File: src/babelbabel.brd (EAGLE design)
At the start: 41 x 75.5 mm, 150 parts, among them CON1 CON-4P-TABS-JST_GH-RA, CON10 CON-6P-SM06B, CON101 PINHEAD_1X04-2.54, CON102 PINHEAD_1X03-2.54, CON11 PINHEAD_1X04-2.54, CON12 PINHEAD_1X06-2.54, CON15 PINHEAD_1X04-2.54, CON16 CON-4P-TABS-JST_GH-RA, CON2 PINHEAD_1X04-2.54, CON201 PINHEAD_1X04-2.54, CON202 PINHEAD_1X03-2.54, CON3 PINHEAD_1X04-2.54, CON4 USB-AA-PTH, CON5 CON-4P-TABS-JST_GH-RA, CON6 CON-4P-TABS-JST_GH-RA, CON7 USB-1, IC1 NS5B1G385, IC101 STM32F373CBT6-LQFP48, IC102 STM32F373RCT6, IC103 AP2127-3.3, IC105 TJA1051-SO8, IC108 TPD3S014DBVR-SOT23-6, IC13 STM32F103CBT7, IC14 74LVC2T45, IC15 74LVC2T45, IC16 74LVC2T45, IC17 74LVC2T45, IC2 NS5B1G385, IC201 STM32F373CBT6-LQFP48, IC202 STM32F373RCT6, IC203 AP2127-3.3, IC205 TJA1051-SO8, IC208 TPD3S014DBVR-SOT23-6, IC3 AP2127-3.3, IC9 FE1.1S, J1 CONNECTION-SMD, J2 CONNECTION-SMD, Q101 16MHz, Q102 2N7002, Q201 16MHz, Q202 2N7002, Q7 8MHz, Q8 12MHz, Q9 NTZD3152PT1G

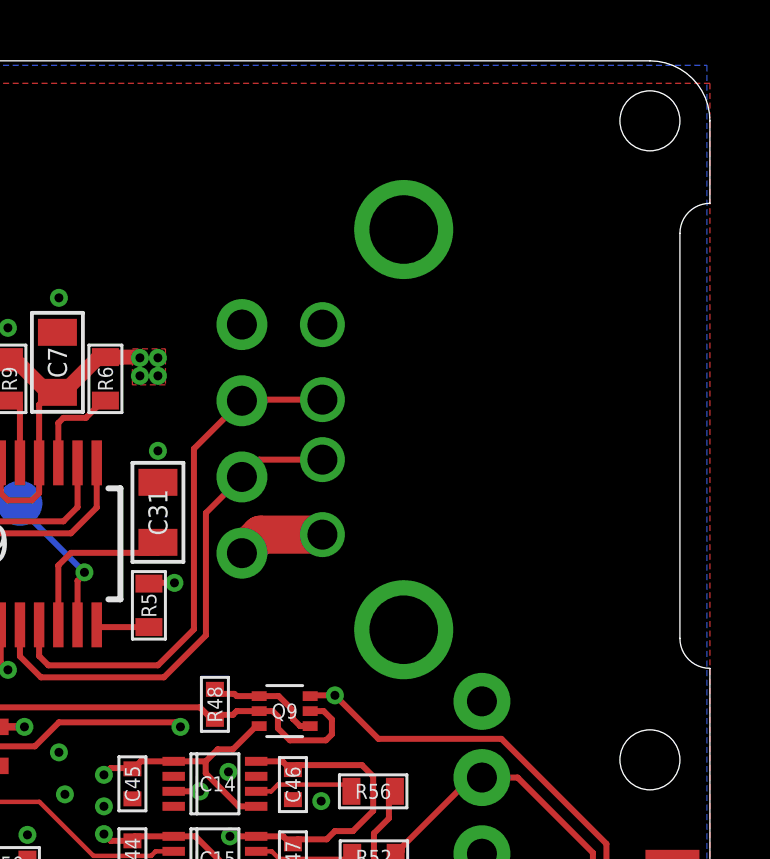
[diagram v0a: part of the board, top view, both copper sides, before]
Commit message: fixed wrong USB connection
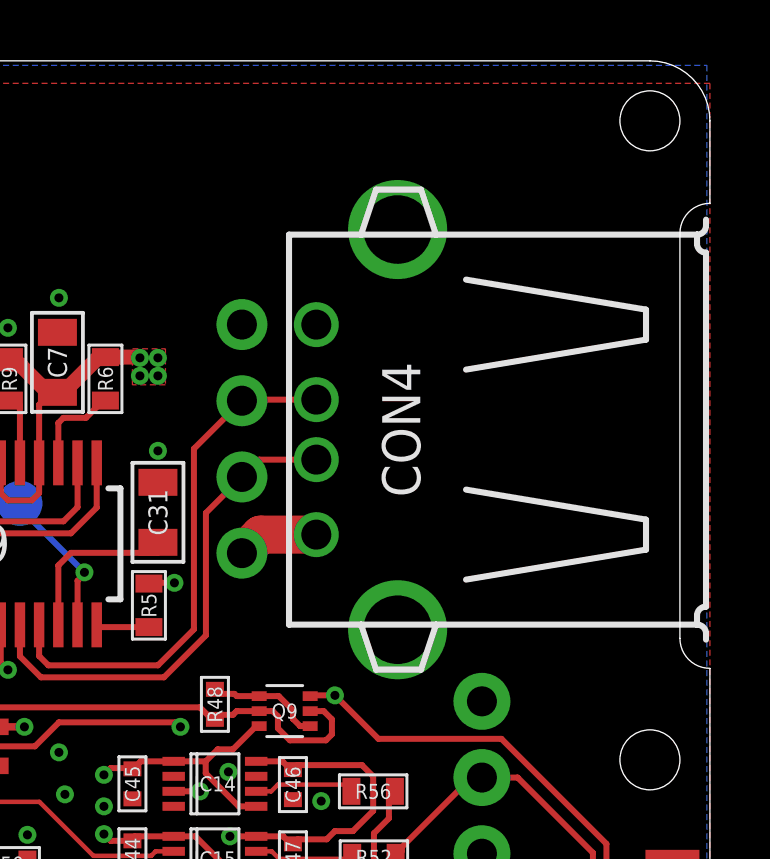
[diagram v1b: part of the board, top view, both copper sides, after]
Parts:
- moved CON4 0.20 mm to (33.2, 25.5), flipped to the top, turned to 90 degrees
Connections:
- net DUT_DM: now also CON4.D-; no longer CON4.D+
- net DUT_DP: now also CON4.D+; no longer CON4.D-
- net GND: now also CON4.GND; no longer CON4.VBUS
- net VDD_5V: now also CON4.VBUS; no longer CON4.GND

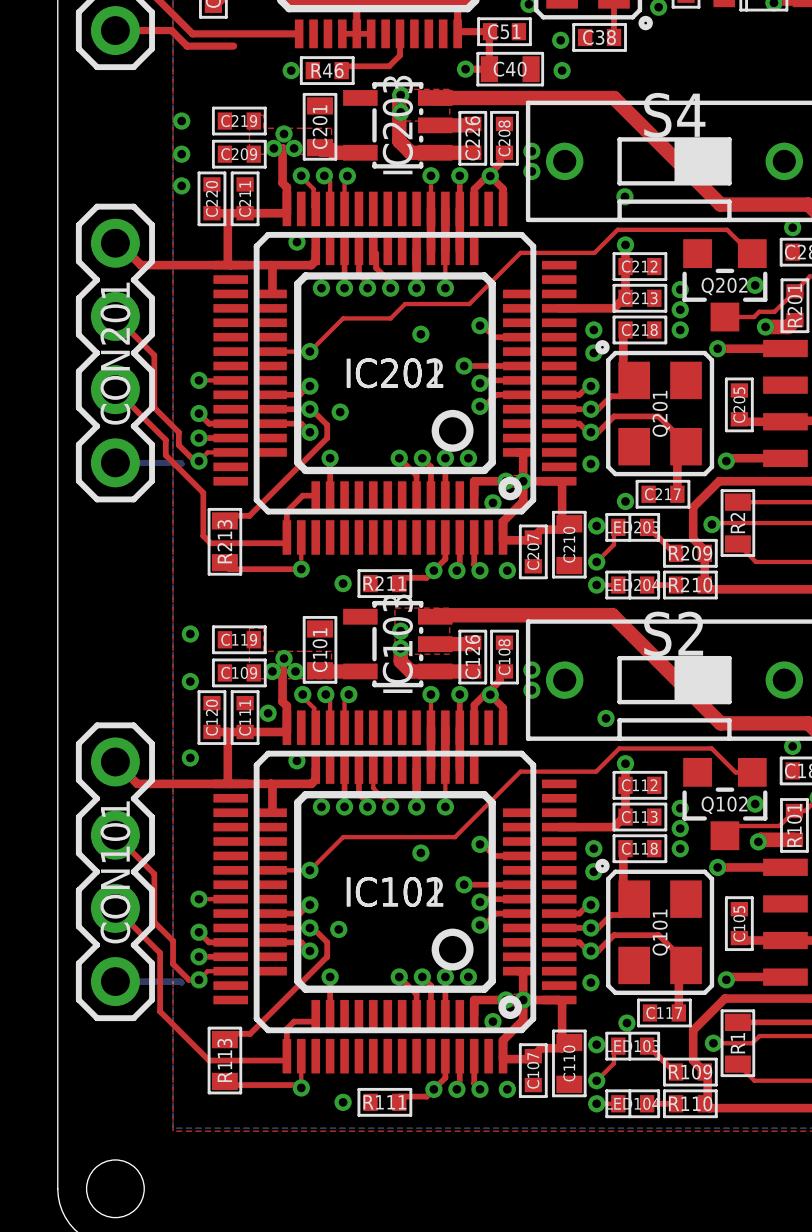
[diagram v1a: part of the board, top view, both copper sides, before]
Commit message: 64 pin swaped with 48
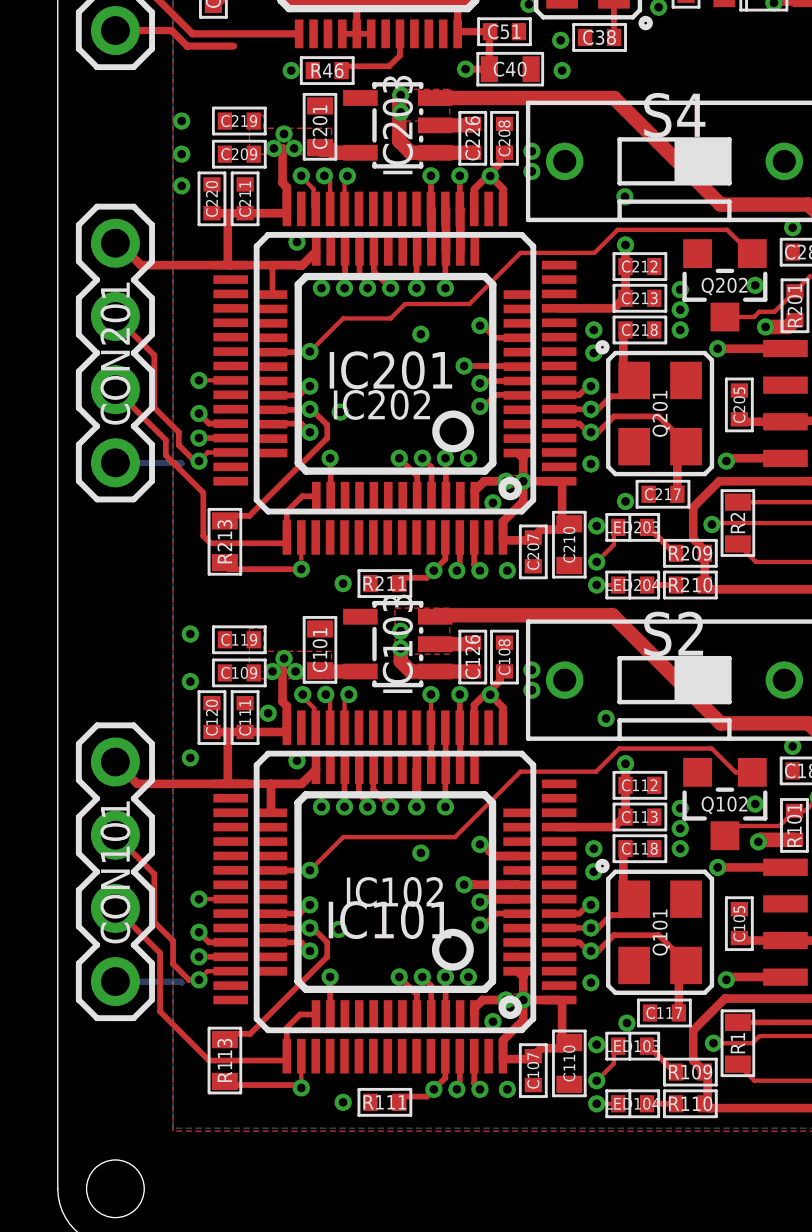
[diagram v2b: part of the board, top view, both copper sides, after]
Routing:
- net BABEL1:PA4: track 25.5 -> 24.0 mm
- net BABEL2:PA6: track 20.2 -> 18.8 mm
- net BABEL2:PA4: track 25.4 -> 24.0 mm
- net BABEL2:VDD_3V3: track 82.9 -> 81.9 mm
- net BABEL1:VDD_3V3: track 83.3 -> 82.2 mm

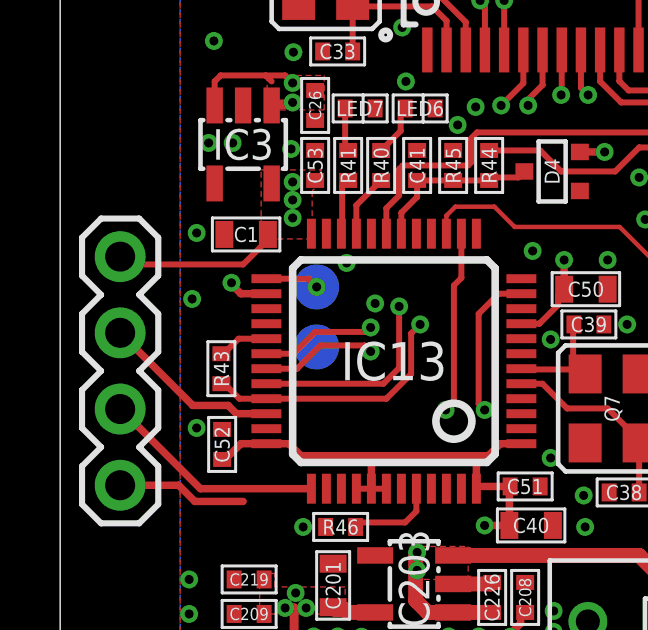
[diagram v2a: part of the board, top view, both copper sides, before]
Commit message: DCP switch pulled high
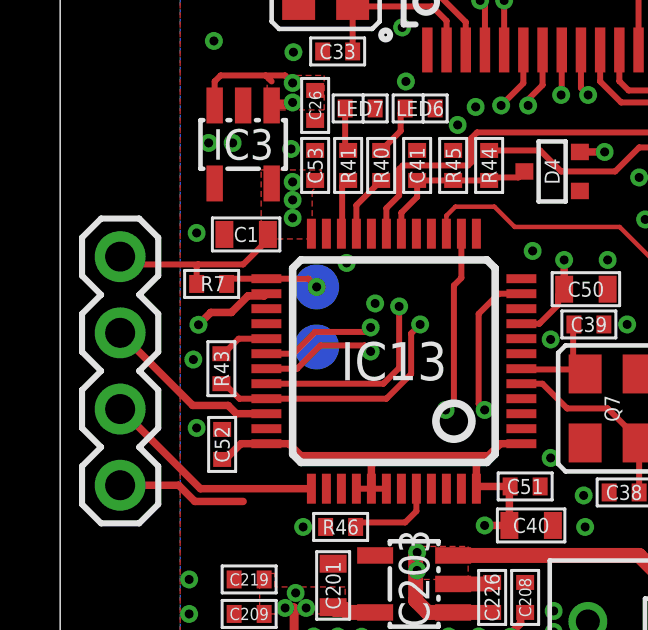
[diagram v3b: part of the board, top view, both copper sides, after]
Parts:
- added R7: 10K, rc:R0402
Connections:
- net SWITCH: now also R7.2
- net VDD_3V3: now also R7.1
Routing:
- net VDD_5V: track 191.6 -> 194.3 mm
- net SWITCH: track 1.79 -> 3.19 mm
- net VDD_3V3: track 82.6 -> 83.3 mm
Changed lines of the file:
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@@
 <attribute name="NAME" x="11.557" y="-7.348" size="1.27" layer="25" font="vector" ratio="15" rot="R180" align="center"/>
+</element>
+<element name="R7" library="rc" library_urn="urn:adsk.eagle:library:2539423" package="R0402" package3d_urn="urn:adsk.eagle:package:2539456/2" value="10K" x="5.05" y="11.15" smashed="yes">
+<attribute name="AEC-Q" value="" x="5.05" y="11.15" size="1.778" layer="27" display="off"/>
+<attribute name="DIGIKEY#" value="" x="5.05" y="11.15" size="1.778" layer="27" display="off"/>
+<attribute name="LCSC#" value="C25744" x="5.05" y="11.15" size="1.778" layer="27" display="off"/>
+<attribute name="MANF" value="" x="5.05" y="11.15" size="1.778" layer="27" display="off"/>
+<attribute name="MANF#" value="" x="5.05" y="11.15" size="1.778" layer="27" display="off"/>
+<attribute name="NAME" x="5.09" y="11.16" size="0.5" layer="25" font="vector" ratio="12" align="center"/>
+<attribute name="OPERATING_TEMP" value="" x="5.05" y="11.15" size="1.778" layer="27" display="off"/>
+<attribute name="PACKAGE" value="0402" x="5.05" y="11.15" size="1.778" layer="27" display="off"/>
+<attribute name="TOLERANCE" value="1%" x="5.05" y="11.15" size="1.778" layer="27" display="off"/>
 </element>
 </elements>
@@
 <via x="28.04283125" y="13.075" extent="1-16" drill="0.3" diameter="0.6"/>
 <via x="28.15" y="7.8" extent="1-16" drill="0.3" diameter="0.6"/>
-<via x="4.4" y="10.65" extent="1-16" drill="0.3" diameter="0.6"/>
+<via x="4.44" y="8.63" extent="1-16" drill="0.3" diameter="0.6"/>
 <via x="10.5" y="10.5" extent="1-16" drill="0.3" diameter="0.6"/>
 <via x="11.4" y="19.7" extent="1-16" drill="0.3" diameter="0.6"/>
@@
 <wire x1="5.5" y1="5.3" x2="5.4" y2="5.3" width="0.25" layer="1"/>
 <wire x1="2" y1="12.06" x2="2.26" y2="11.8" width="0.2" layer="1"/>
-<wire x1="2.26" y1="11.8" x2="6.1" y2="11.8" width="0.2" layer="1"/>
+<wire x1="2.26" y1="11.8" x2="4.6" y2="11.8" width="0.2" layer="1"/>
+<wire x1="4.6" y1="11.8" x2="6.1" y2="11.8" width="0.2" layer="1"/>
 <wire x1="6.925" y1="12.625" x2="6.925" y2="12.8" width="0.2" layer="1"/>
 <wire x1="6.1" y1="11.8" x2="6.925" y2="12.625" width="0.2" layer="1"/>
@@
 <wire x1="24.59283125" y1="14.8" x2="24.19283125" y2="14.4" width="0.2" layer="1"/>
 <wire x1="25.1" y1="14.8" x2="24.59283125" y2="14.8" width="0.2" layer="1"/>
+<contactref element="R7" pad="1"/>
+<wire x1="4.55" y1="11.15" x2="4.55" y2="11.75" width="0.2" layer="1"/>
+<wire x1="4.55" y1="11.75" x2="4.6" y2="11.8" width="0.2" layer="1"/>
 </signal>
 <signal name="DCP_DM">
@@
 <wire x1="6.6" y1="20.65" x2="13.5" y2="27.55" width="0.6" layer="15"/>
 <wire x1="6.6" y1="-3.8" x2="6.6" y2="2.2" width="0.6" layer="15"/>
-<wire x1="6.6" y1="2.2" x2="6.6" y2="11.188909375" width="0.6" layer="15"/>
-<wire x1="6.6" y1="11.188909375" x2="6.6" y2="17.8" width="0.6" layer="15"/>
+<wire x1="6.6" y1="2.2" x2="6.6" y2="10.32" width="0.6" layer="15"/>
+<wire x1="6.6" y1="10.32" x2="6.6" y2="17.8" width="0.6" layer="15"/>
 <wire x1="6.6" y1="17.8" x2="6.6" y2="20.65" width="0.6" layer="15"/>
 <wire x1="11.9" y1="2.2" x2="6.6" y2="2.2" width="0.6" layer="15"/>
@@
 <wire x1="7.05" y1="17.1" x2="7.65" y2="17.1" width="0.25" layer="1"/>
 <wire x1="7.65" y1="17.1" x2="7.75" y2="17.2" width="0.25" layer="1"/>
-<wire x1="6.875" y1="10.825" x2="6.025" y2="10.825" width="0.25" layer="1"/>
-<wire x1="6.025" y1="10.825" x2="5.711090625" y2="11.138909375" width="0.25" layer="1"/>
-<wire x1="5.711090625" y1="11.138909375" x2="5.711090625" y2="11.188909375" width="0.25" layer="1"/>
-<via x="5.711090625" y="11.188909375" extent="1-16" drill="0.3" diameter="0.6"/>
+<via x="4.611090625" y="9.788909375" extent="1-16" drill="0.3" diameter="0.6"/>
 <wire x1="5.15" y1="17.1" x2="5.15" y2="17.9" width="0.2" layer="1"/>
 <wire x1="5.15" y1="17.9" x2="5.35" y2="18.1" width="0.2" layer="1"/>
-<wire x1="5.711090625" y1="11.188909375" x2="6.6" y2="11.188909375" width="0.2" layer="15"/>
 <wire x1="5.35" y1="18.1" x2="7.5" y2="18.1" width="0.2" layer="1"/>
 <wire x1="7.5" y1="18.1" x2="7.75" y2="17.85" width="0.2" layer="1"/>
@@
 <wire x1="25.4" y1="21.34" x2="26.0169" y2="21.9569" width="1.27" layer="1"/>
 <wire x1="26.0169" y1="21.9569" x2="27.8799" y2="21.9569" width="1.27" layer="1"/>
+<wire x1="4.611090625" y1="9.788909375" x2="6.068909375" y2="9.788909375" width="0.3048" layer="15"/>
+<wire x1="6.068909375" y1="9.788909375" x2="6.6" y2="10.32" width="0.3048" layer="15"/>
+<wire x1="6.875" y1="10.825" x2="6.802" y2="10.752" width="0.254" layer="1"/>
+<wire x1="6.802" y1="10.752" x2="6.2602625" y2="10.752" width="0.254" layer="1"/>
+<wire x1="6.2602625" y1="10.752" x2="5.7082625" y2="10.2" width="0.254" layer="1"/>
+<wire x1="5.02218125" y1="10.2" x2="4.611090625" y2="9.788909375" width="0.254" layer="1"/>
+<wire x1="5.7082625" y1="10.2" x2="5.02218125" y2="10.2" width="0.254" layer="1"/>
 </signal>
 <signal name="N$37">
@@
 <wire x1="8.275" y1="11.325" x2="6.875" y2="11.325" width="0.2" layer="1"/>
 <via x="8.55" y="11.05" extent="1-16" drill="0.3" diameter="0.6"/>
+<contactref element="R7" pad="2"/>
+<wire x1="6.875" y1="11.325" x2="5.725" y2="11.325" width="0.2" layer="1"/>
+<wire x1="5.725" y1="11.325" x2="5.55" y2="11.15" width="0.2" layer="1"/>
 </signal>
 <signal name="N$39">
